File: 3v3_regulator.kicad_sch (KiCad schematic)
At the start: 5 parts, among them U2 AP2112K-3.3TRG1

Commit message: laid out stuff
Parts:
- U2: Availability In Stock -> (none); Check_prices https://www.snapeda.com/parts/AP2112K-3.3TRG1/Diodes+Inc./v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 -> (none); MANUFACTURER Diodes Inc. -> (none); MF Diodes Inc. -> (none); MP AP2112K-3.3TRG1 -> (none); PARTREV 2-2 -> (none); Package SOT-753 Diodes Inc. -> (none); Price None -> (none); Purchase-URL https://www.snapeda.com/api/url_track_click_mouser/?unipart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 -> (none); SnapEDA_Link https://www.snapeda.com/parts/AP2112K-3.3TRG1/Diodes+Inc./v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 -> (none)
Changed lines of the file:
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@@
 (kicad_sch (version 20230121) (generator eeschema)
-  (paper "A4")
+  (paper "USLetter")
+  (title_block
+    (date "2024-01-01")
+    (rev "A01")
+  )
   (junction (at 107.95 100.33) (diameter 0) (color 0 0 0 0)
   )
@@
       (effects (font (size 1.27 1.27)) hide)
     )
+    (property "Digikey PN" "" (at 117.475 104.14 0)
+      (effects (font (size 1.27 1.27)) hide)
+    )
     (pin "1")
     (pin "2")
@@
     )
     (property "Datasheet" "~" (at 107.95 104.14 0)
+      (effects (font (size 1.27 1.27)) hide)
+    )
+    (property "Digikey PN" "" (at 107.95 104.14 0)
       (effects (font (size 1.27 1.27)) hide)
     )
@@
     )
     (property "Datasheet" "~" (at 107.95 111.76 0)
+      (effects (font (size 1.27 1.27)) hide)
+    )
+    (property "Digikey PN" "" (at 107.95 111.76 0)
       (effects (font (size 1.27 1.27)) hide)
     )
@@
       (effects (font (size 1.27 1.27)) hide)
     )
+    (property "Digikey PN" "" (at 144.78 100.965 0)
+      (effects (font (size 1.27 1.27)) hide)
+    )
     (pin "1")
     (pin "2")
@@
       (effects (font (size 1.27 1.27)) hide)
     )
-    (property "MF" "Diodes Inc." (at 130.175 100.33 0)
-      (effects (font (size 1.27 1.27)) (justify bottom) hide)
-    )
-    (property "Description" "\nVoltage Regulators, LDO, 600mA CMOS LDO 50mA 3.3V 250mV | Diodes Inc AP2112K-3.3TRG1\n" (at 130.175 88.9 0)
-      (effects (font (size 1.27 1.27)) (justify bottom) hide)
-    )
-    (property "Package" "SOT-753 Diodes Inc." (at 130.175 87.63 0)
-      (effects (font (size 1.27 1.27)) (justify bottom) hide)
-    )
-    (property "Price" "None" (at 130.175 100.33 0)
-      (effects (font (size 1.27 1.27)) (justify bottom) hide)
-    )
-    (property "Check_prices" "https://www.snapeda.com/parts/AP2112K-3.3TRG1/Diodes+Inc./view-part/?ref=eda" (at 130.175 86.36 0)
-      (effects (font (size 1.27 1.27)) (justify bottom) hide)
-    )
-    (property "PARTREV" "2-2" (at 128.905 87.63 0)
-      (effects (font (size 1.27 1.27)) (justify bottom) hide)
-    )
-    (property "SnapEDA_Link" "https://www.snapeda.com/parts/AP2112K-3.3TRG1/Diodes+Inc./view-part/?ref=snap" (at 130.175 100.33 0)
-      (effects (font (size 1.27 1.27)) (justify bottom) hide)
-    )
-    (property "MP" "AP2112K-3.3TRG1" (at 130.175 100.33 0)
-      (effects (font (size 1.27 1.27)) (justify bottom) hide)
-    )
-    (property "Purchase-URL" "https://www.snapeda.com/api/url_track_click_mouser/?unipart_id=454988&manufacturer=Diodes Inc.&part_name=AP2112K-3.3TRG1&search_term=None" (at 130.175 87.63 0)
-      (effects (font (size 1.27 1.27)) (justify bottom) hide)
-    )
-    (property "Availability" "In Stock" (at 130.175 100.33 0)
-      (effects (font (size 1.27 1.27)) (justify bottom) hide)
-    )
-    (property "MANUFACTURER" "Diodes Inc." (at 130.175 100.33 0)
-      (effects (font (size 1.27 1.27)) (justify bottom) hide)
-    )
-    (pin "1")
+    (property "Digikey PN" "" (at 130.175 100.33 0)
+      (effects (font (size 1.27 1.27)) hide)
+    )
+    (pin "1")

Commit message: neat-ified schematics
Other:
- company: (none) -> The Art and Science of PCB Design
- title: (none) -> RGB LED Driver Demo Board
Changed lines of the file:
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@@
   (paper "USLetter")
   (title_block
+    (title "RGB LED Driver Demo Board")
     (date "2024-01-01")
     (rev "A01")
+    (company "The Art and Science of PCB Design")
   )
   (junction (at 107.95 100.33) (diameter 0) (color 0 0 0 0)

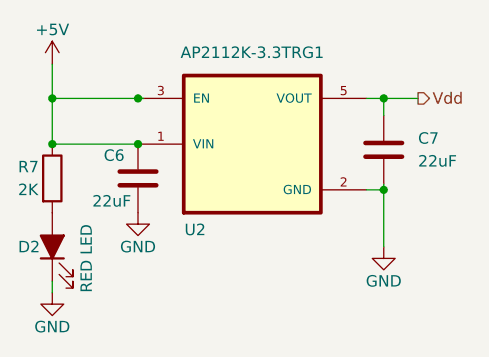
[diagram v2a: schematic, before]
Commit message: Added annotations, BOM count reduction
LED indicator resistors edited to save on BOM count

schematics made more neat, added some labels
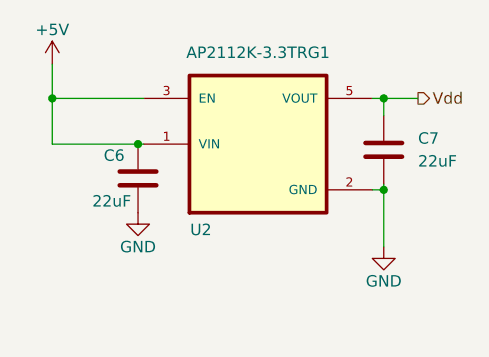
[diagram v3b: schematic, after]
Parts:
- removed D2: RED LED, LED_SMD:LED_0805_2012Metric_Pad1.15x1.40mm_HandSolder, symbol Device:LED_Filled
- removed R7: 2K, Resistor_SMD:R_0805_2012Metric_Pad1.20x1.40mm_HandSolder, symbol Device:R
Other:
- moved on the sheet: U2
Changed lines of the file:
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@@
     (company "The Art and Science of PCB Design")
-  )
-  (junction (at 107.95 100.33) (diameter 0) (color 0 0 0 0)
-  )
-  (junction (at 117.475 95.25) (diameter 0) (color 0 0 0 0)
   )
   (junction (at 117.475 100.33) (diameter 0) (color 0 0 0 0)
@@
     (stroke (width 0) (type default))
   )
-  (wire (pts (xy 118.11 95.25) (xy 117.475 95.25))
-    (stroke (width 0) (type default))
-  )
-  (wire (pts (xy 142.875 95.25) (xy 144.78 95.25))
+  (wire (pts (xy 143.51 95.25) (xy 144.78 95.25))
     (stroke (width 0) (type default))
   )
@@
     (stroke (width 0) (type default))
   )
-  (wire (pts (xy 117.475 95.25) (xy 107.95 95.25))
-    (stroke (width 0) (type default))
-  )
-  (wire (pts (xy 107.95 115.57) (xy 107.95 116.84))
-    (stroke (width 0) (type default))
-  )
   (wire (pts (xy 144.78 104.775) (xy 144.78 105.41))
     (stroke (width 0) (type default))
   )
-  (wire (pts (xy 142.875 105.41) (xy 144.78 105.41))
+  (wire (pts (xy 143.51 105.41) (xy 144.78 105.41))
     (stroke (width 0) (type default))
   )
@@
     (stroke (width 0) (type default))
   )
+  (wire (pts (xy 118.11 100.33) (xy 117.475 100.33))
+    (stroke (width 0) (type default))
+  )
   (wire (pts (xy 144.78 95.25) (xy 148.59 95.25))
+    (stroke (width 0) (type default))
+  )
+  (wire (pts (xy 107.95 95.25) (xy 118.11 95.25))
     (stroke (width 0) (type default))
   )
@@
     )
   )
-  (symbol (lib_id "Device:R") (at 107.95 104.14 0) (unit 1)
-    (in_bom yes) (on_board yes) (dnp no)
-    (property "Reference" "R7" (at 104.14 102.87 0)
-      (effects (font (size 1.27 1.27)) (justify left))
-    )
-    (property "Value" "2K" (at 104.14 105.41 0)
-      (effects (font (size 1.27 1.27)) (justify left))
-    )
-    (property "Footprint" "Resistor_SMD:R_0805_2012Metric_Pad1.20x1.40mm_HandSolder" (at 106.172 104.14 90)
-      (effects (font (size 1.27 1.27)) hide)
-    )
-    (property "Datasheet" "~" (at 107.95 104.14 0)
-      (effects (font (size 1.27 1.27)) hide)
-    )
-    (property "Digikey PN" "" (at 107.95 104.14 0)
-      (effects (font (size 1.27 1.27)) hide)
-    )
-    (pin "1")
-    (pin "2")
-    (instances
-      (project "RGB LED Driver"
-        (path "/955dc1f6-0512-416a-b86b-95ec08ff77cb/deba0225-9fd5-4c57-9c6a-a09255a1b7d0"
-          (reference "R7") (unit 1)
-        )
-      )
-    )
-  )
-  (symbol (lib_id "power:GND") (at 107.95 116.84 0) (unit 1)
-    (in_bom yes) (on_board yes) (dnp no)
-    (property "Reference" "#PWR06" (at 107.95 123.19 0)
-      (effects (font (size 1.27 1.27)) hide)
-    )
-    (property "Value" "GND" (at 107.95 120.65 0)
-      (effects (font (size 1.27 1.27)))
-    )
-    (property "Footprint" "" (at 107.95 116.84 0)
-      (effects (font (size 1.27 1.27)) hide)
-    )
-    (property "Datasheet" "" (at 107.95 116.84 0)
-      (effects (font (size 1.27 1.27)) hide)
-    )
-    (pin "1")
-    (instances
-      (project "RGB LED Driver"
-        (path "/955dc1f6-0512-416a-b86b-95ec08ff77cb/deba0225-9fd5-4c57-9c6a-a09255a1b7d0"
-          (reference "#PWR06") (unit 1)
-        )
-      )
-    )
-  )
-  (symbol (lib_id "Device:LED_Filled") (at 107.95 111.76 90) (unit 1)
-    (in_bom yes) (on_board yes) (dnp no)
-    (property "Reference" "D2" (at 104.14 111.76 90)
-      (effects (font (size 1.27 1.27)) (justify right))
-    )
-    (property "Value" "RED LED" (at 111.76 109.22 0)
-      (effects (font (size 1.27 1.27)) (justify right))
-    )
-    (property "Footprint" "LED_SMD:LED_0805_2012Metric_Pad1.15x1.40mm_HandSolder" (at 107.95 111.76 0)
-      (effects (font (size 1.27 1.27)) hide)
-    )
-    (property "Datasheet" "~" (at 107.95 111.76 0)
-      (effects (font (size 1.27 1.27)) hide)
-    )
-    (property "Digikey PN" "" (at 107.95 111.76 0)
-      (effects (font (size 1.27 1.27)) hide)
-    )
-    (pin "1")
-    (pin "2")
-    (instances
-      (project "RGB LED Driver"
-        (path "/955dc1f6-0512-416a-b86b-95ec08ff77cb/deba0225-9fd5-4c57-9c6a-a09255a1b7d0"
-          (reference "D2") (unit 1)
-        )
-      )
-    )
-  )
   (symbol (lib_id "Device:C") (at 144.78 100.965 0) (unit 1)
     (in_bom yes) (on_board yes) (dnp no) (fields_autoplaced)
@@
     )
   )
-  (symbol (lib_id "AP2112K-3.3TRG1:AP2112K-3.3TRG1") (at 130.175 100.33 0) (unit 1)
+  (symbol (lib_id "AP2112K-3.3TRG1:AP2112K-3.3TRG1") (at 130.81 100.33 0) (unit 1)
     (in_bom yes) (on_board yes) (dnp no)
-    (property "Reference" "U2" (at 123.825 109.855 0)
+    (property "Reference" "U2" (at 124.46 109.855 0)
       (effects (font (size 1.27 1.27)))
     )
-    (property "Value" "AP2112K-3.3TRG1" (at 130.175 90.17 0)
+    (property "Value" "AP2112K-3.3TRG1" (at 130.81 90.17 0)
       (effects (font (size 1.27 1.27)))
     )
-    (property "Footprint" "Package_TO_SOT_SMD:SOT-23-5_HandSoldering" (at 130.175 88.9 0)
+    (property "Footprint" "Package_TO_SOT_SMD:SOT-23-5_HandSoldering" (at 130.81 88.9 0)
       (effects (font (size 1.27 1.27)) (justify bottom) hide)
     )
-    (property "Datasheet" "" (at 130.175 100.33 0)
+    (property "Datasheet" "" (at 130.81 100.33 0)
       (effects (font (size 1.27 1.27)) hide)
     )
-    (property "Digikey PN" "" (at 130.175 100.33 0)
+    (property "Digikey PN" "" (at 130.81 100.33 0)
       (effects (font (size 1.27 1.27)) hide)
     )

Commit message: added digikey PNs
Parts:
- C6, C7: Digikey PN (none) -> 1276-2910-1-ND; MPN (none) -> CL21A226MPQNNNE
- U2: Digikey PN (none) -> AP2112K-3.3TRG1DICT-ND; MPN (none) -> AP2112K-3.3TRG1
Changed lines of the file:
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@@
       (effects (font (size 1.27 1.27)) hide)
     )
-    (property "Digikey PN" "" (at 117.475 104.14 0)
+    (property "Digikey PN" "1276-2910-1-ND" (at 117.475 104.14 0)
+      (effects (font (size 1.27 1.27)) hide)
+    )
+    (property "MPN" "CL21A226MPQNNNE" (at 117.475 104.14 0)
       (effects (font (size 1.27 1.27)) hide)
     )
@@
       (effects (font (size 1.27 1.27)) hide)
     )
-    (property "Digikey PN" "" (at 144.78 100.965 0)
+    (property "Digikey PN" "1276-2910-1-ND" (at 144.78 100.965 0)
+      (effects (font (size 1.27 1.27)) hide)
+    )
+    (property "MPN" "CL21A226MPQNNNE" (at 144.78 100.965 0)
       (effects (font (size 1.27 1.27)) hide)
     )
@@
       (effects (font (size 1.27 1.27)) hide)
     )
-    (property "Digikey PN" "" (at 130.81 100.33 0)
+    (property "Digikey PN" "AP2112K-3.3TRG1DICT-ND" (at 130.81 100.33 0)
       (effects (font (size 1.27 1.27)) hide)
     )
+    (property "MPN" "AP2112K-3.3TRG1" (at 130.81 100.33 0)
+      (effects (font (size 1.27 1.27)) hide)
+    )
